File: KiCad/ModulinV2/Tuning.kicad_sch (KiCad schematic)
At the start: 26 parts

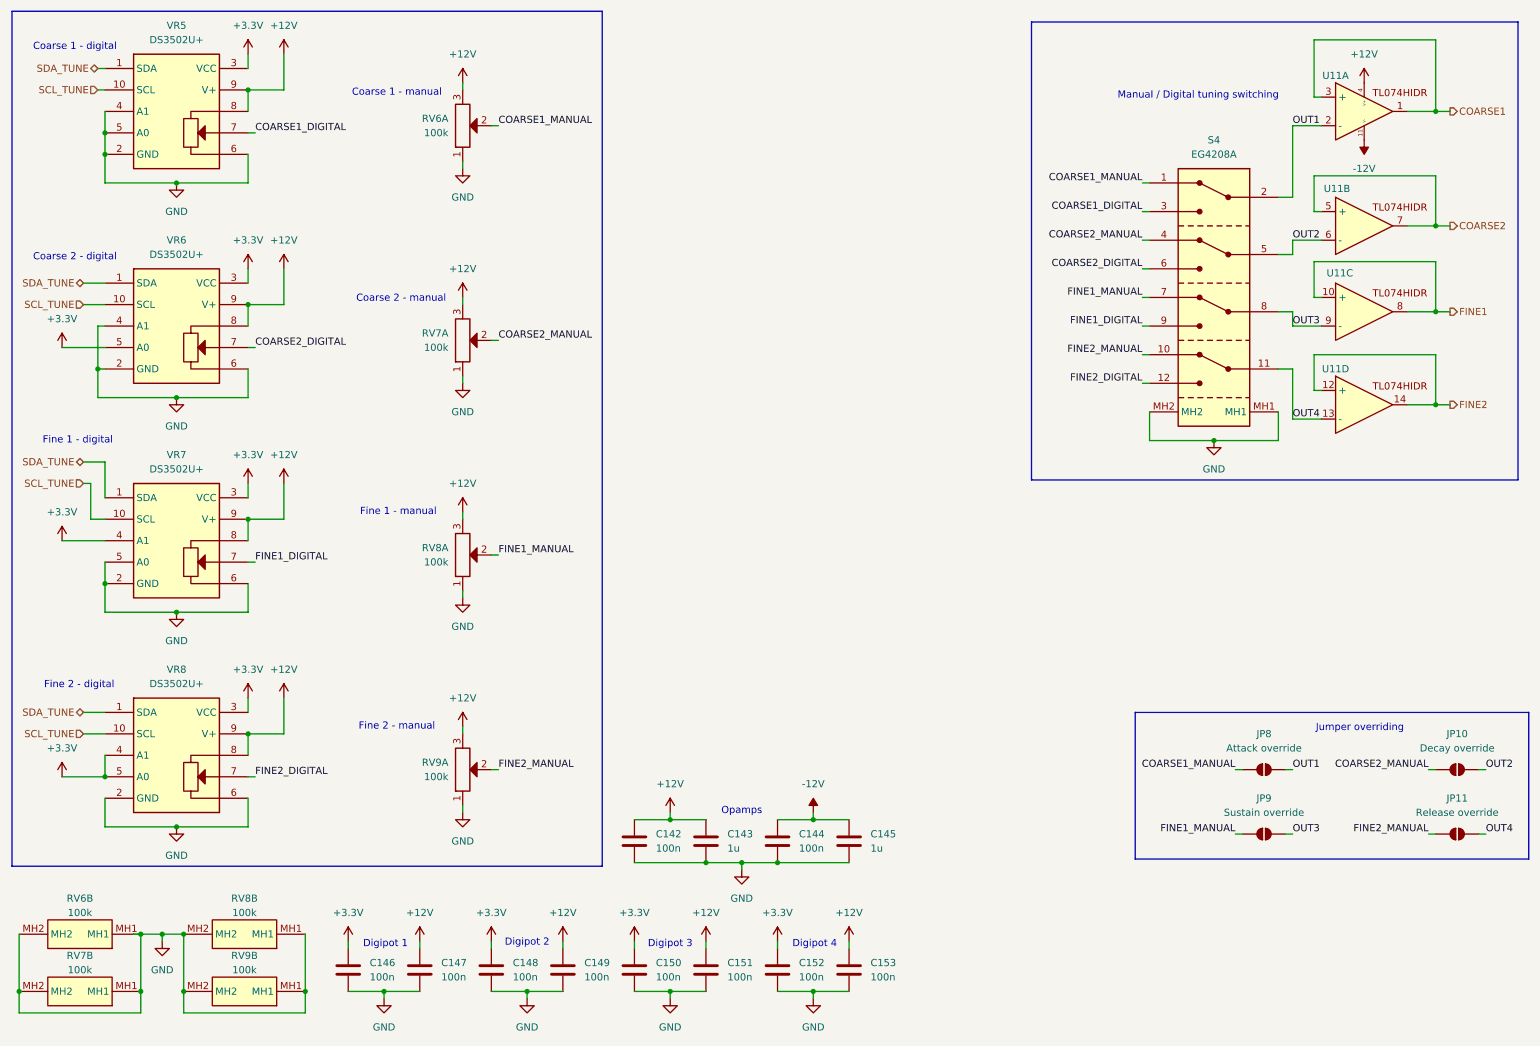
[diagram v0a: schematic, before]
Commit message: Added 4k7 pullups to I2C lines
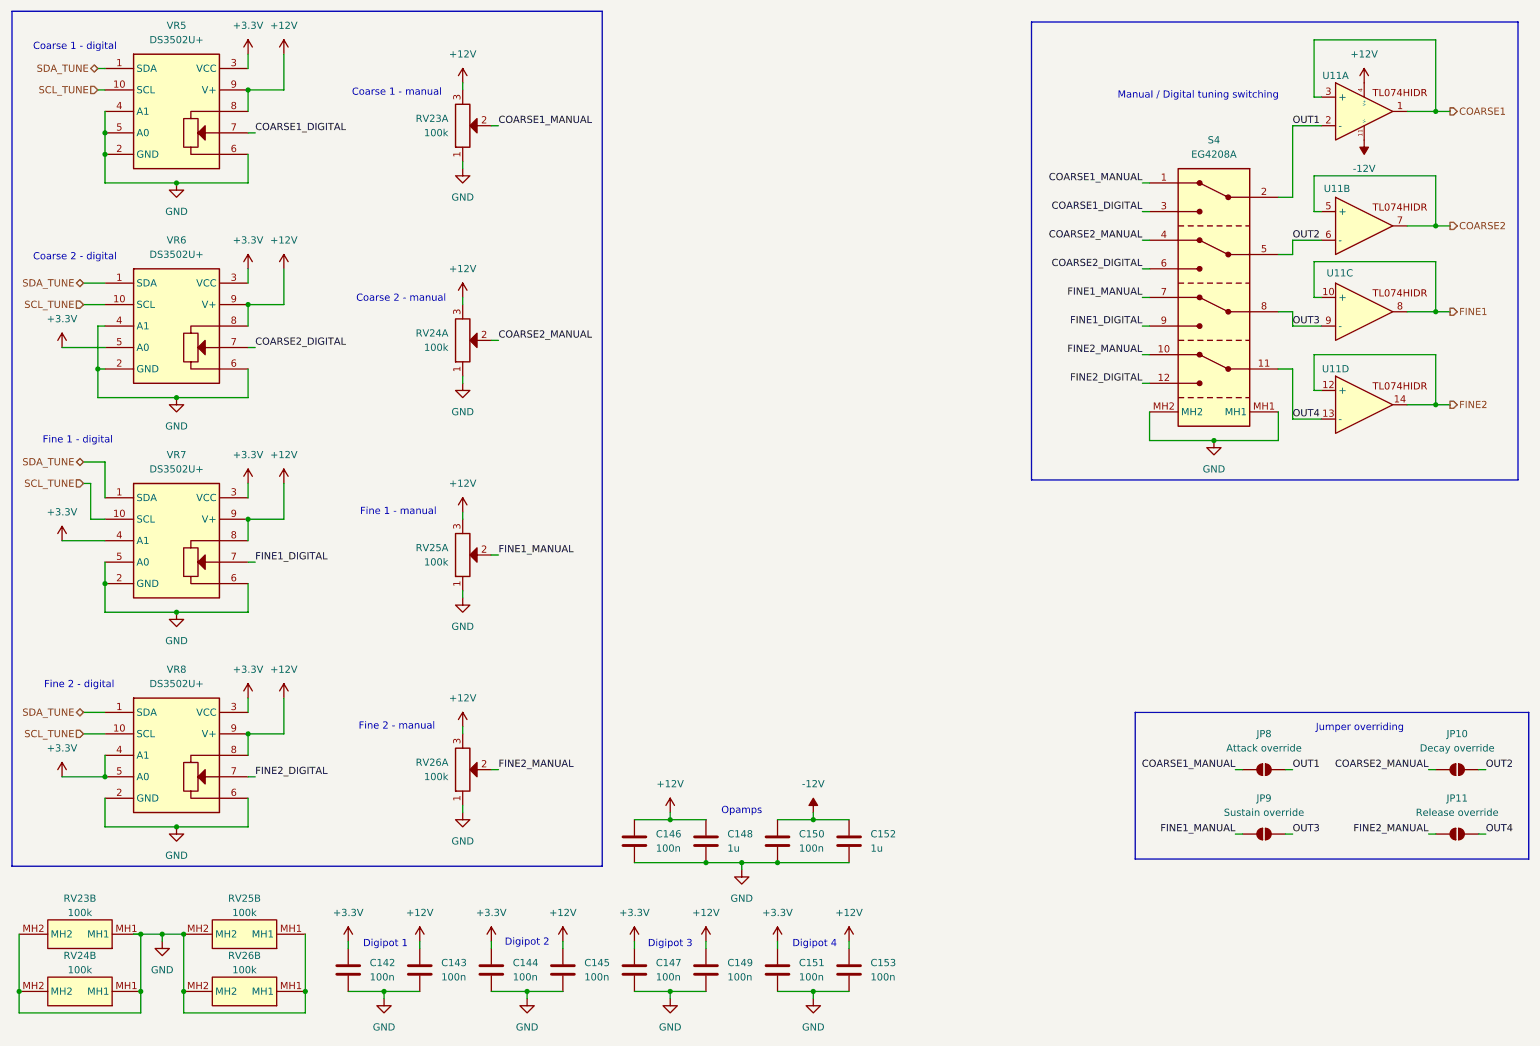
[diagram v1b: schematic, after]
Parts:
- renumbered C146 to C142, C147 to C143, C148 to C144, C149 to C145, C142 to C146, C150 to C147, C143 to C148, C151 to C149, C144 to C150, C152 to C151, C145 to C152, RV6 to RV23, RV7 to RV24, RV8 to RV25, RV9 to RV26

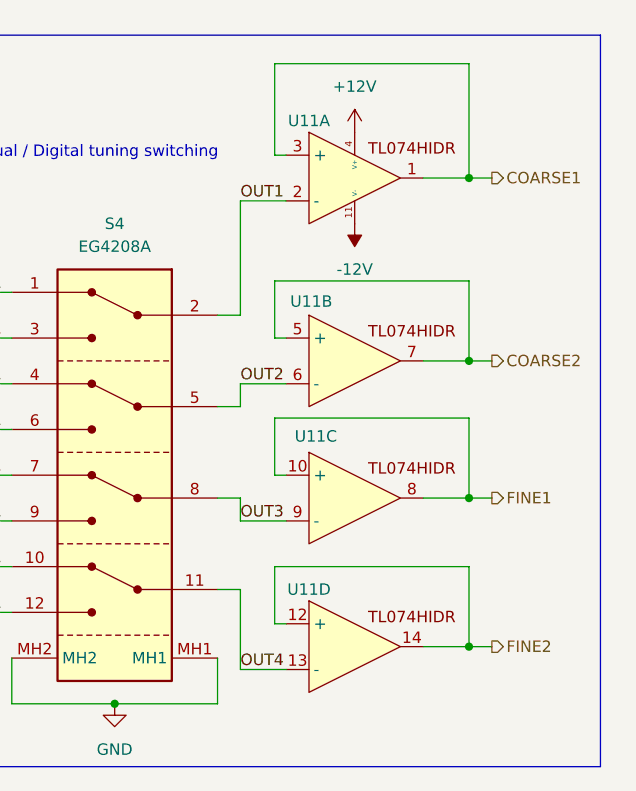
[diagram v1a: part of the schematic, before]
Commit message: Updated TL074 and 72 symbols
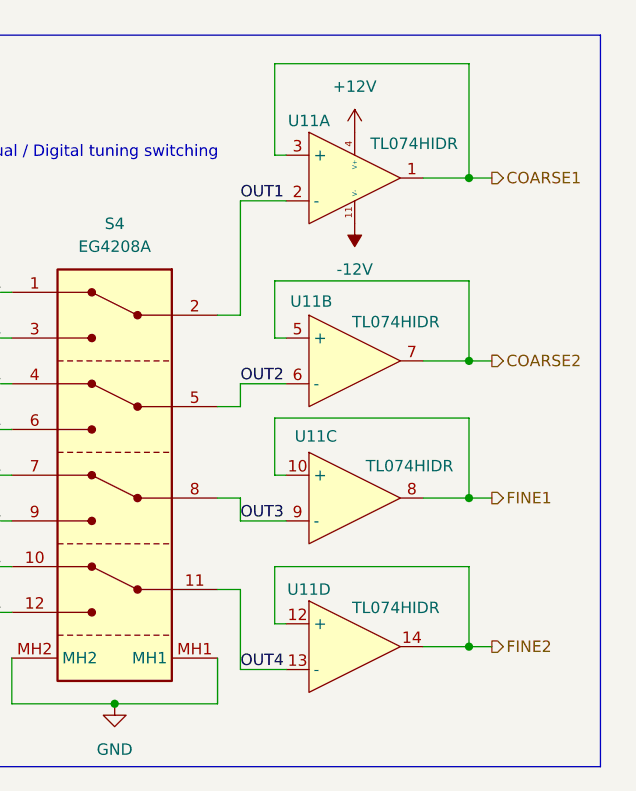
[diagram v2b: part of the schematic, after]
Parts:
- U11: value ~ -> TL074HIDR
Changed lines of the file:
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@@
 			)
 		)
-		(property "Value" "~"
-			(at 257.2155 45.72 0)
+		(property "Value" "TL074HIDR"
+			(at 258.572 47.752 0)
 			(effects
 				(font
@@
 			)
 		)
-		(property "Value" "~"
-			(at 257.2155 60.96 0)
+		(property "Value" "TL074HIDR"
+			(at 260.096 63.754 0)
 			(effects
 				(font
@@
 		(on_board yes)
 		(dnp no)
-		(fields_autoplaced yes)
 		(property "Reference" "U11"
 			(at 248.92 25.4 0)
@@
 			)
 		)
-		(property "Value" "~"
-			(at 266.7 28.5049 0)
+		(property "Value" "TL074HIDR"
+			(at 260.604 27.94 0)
 			(effects
 				(font
@@
 		(on_board yes)
 		(dnp no)
-		(fields_autoplaced yes)
 		(property "Reference" "U11"
 			(at 248.92 77.47 0)
@@
 			)
 		)
-		(property "Value" "~"
-			(at 257.2155 77.47 0)
+		(property "Value" "TL074HIDR"
+			(at 258.572 79.502 0)
 			(effects
 				(font

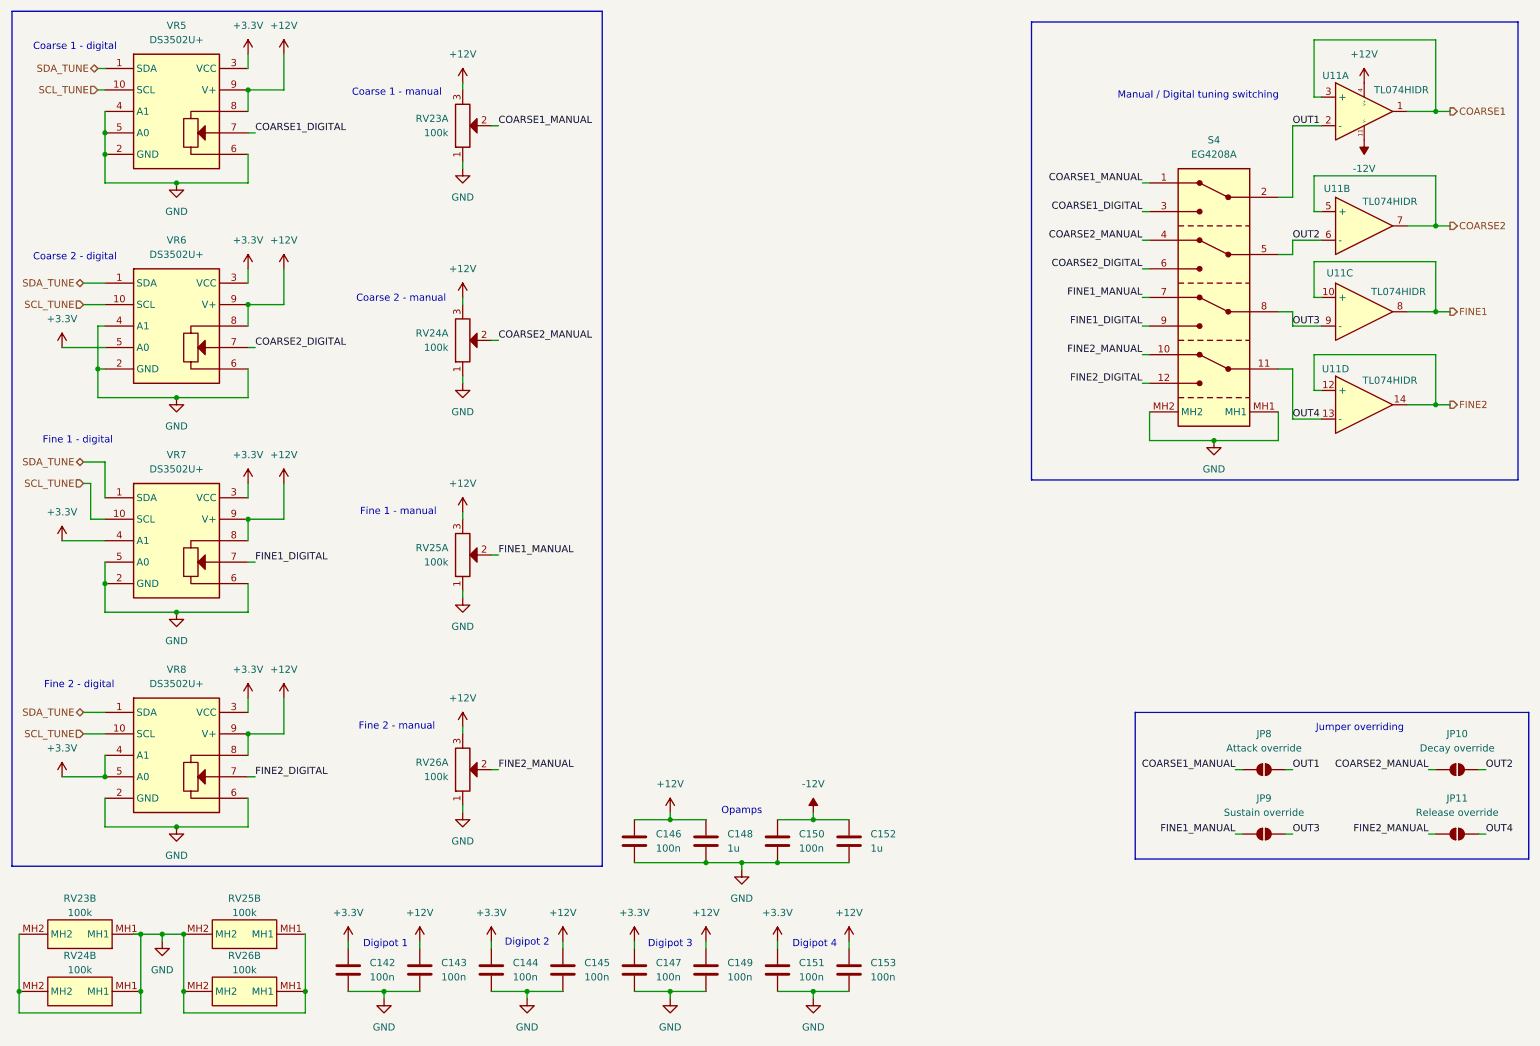
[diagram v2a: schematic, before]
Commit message: Fixed library issues and assigned most footprints
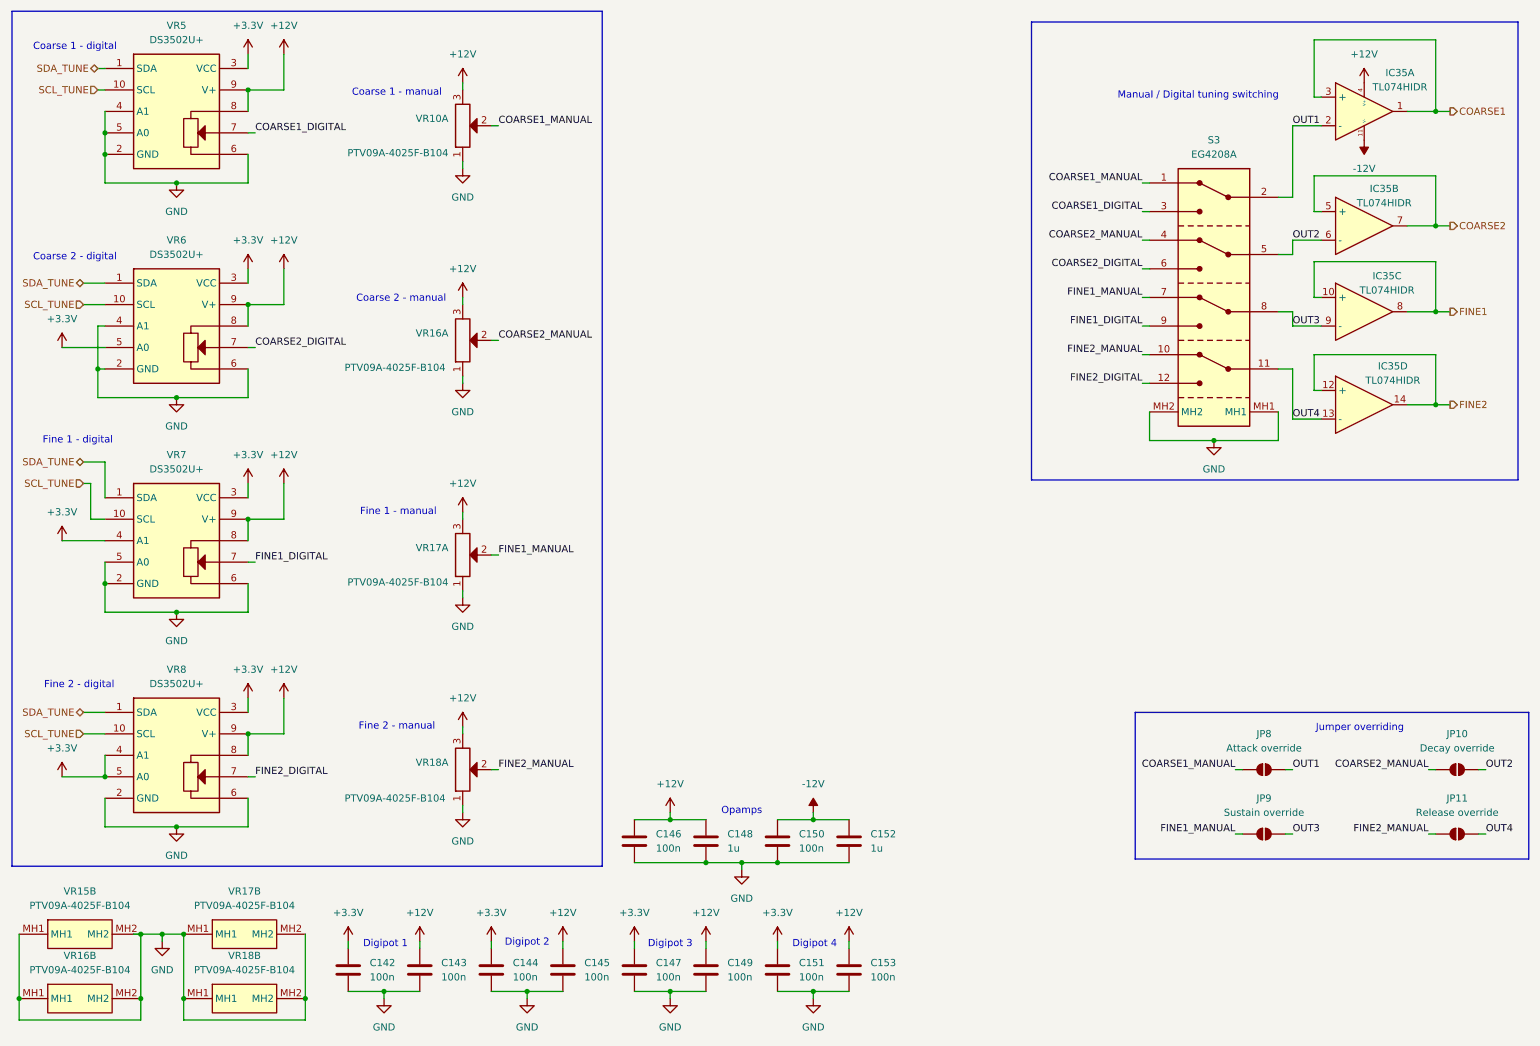
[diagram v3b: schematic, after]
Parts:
- removed RV23, RV24, RV25, RV26: 100k, symbol PTV09A-4025F-B104:PTV09A-4025F-B104_Alt
- removed S4: EG4208A, EG4208A, symbol EG4208A:EG4208A
- removed U11: TL074HIDR, symbol TL074HIDR:TL074HIDRx4
- removed VR5, VR6, VR7, VR8: DS3502U+, SOP50P490X110-10N, symbol DS3502U+:DS3502U+
- added IC35: TL074HIDR, SamacSys_Parts:SOIC127P600X175-14N, symbol SamacSys_Parts:TL074HIDR
- added S3: EG4208A, SamacSys_Parts:EG4208A, symbol SamacSys_Parts:EG4208A
- added VR10, VR15, VR16, VR17, VR18: PTV09A-4025F-B104, SamacSys_Parts:PTV09A4025FB104, symbol SamacSys_Parts:PTV09A-4025F-B104
- added VR5, VR6, VR7, VR8: DS3502U+, SamacSys_Parts:SOP50P490X110-10N, symbol SamacSys_Parts:DS3502U+
- JP10, JP11, JP8, JP9: footprint (none) -> Jumper:SolderJumper-2_P1.3mm_Open_TrianglePad1.0x1.5mm
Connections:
- net +12V: now also IC35.4 (V+), VR10.3, VR16.3, VR17.3, VR18.3, VR5.8, VR5.9 (V+), VR6.8, VR6.9 (V+), VR7.8, VR7.9 (V+), VR8.8, VR8.9 (V+)
- net +3.3V: now also VR5.3 (VCC), VR6.3 (VCC), VR6.5 (A0), VR7.3 (VCC), VR7.4 (A1), VR8.3 (VCC), VR8.4 (A1), VR8.5 (A0)
- net -12V: now also IC35.11 (V-)
- net COARSE1: now also IC35.1, IC35.3 (+)
- net COARSE1_DIGITAL: now also S3.3, VR5.7
- net COARSE1_MANUAL: now also S3.1, VR10.2
- net COARSE2: now also IC35.5 (+), IC35.7
- net COARSE2_DIGITAL: now also S3.6, VR6.7
- net COARSE2_MANUAL: now also S3.4, VR16.2
- net FINE1: now also IC35.10 (+), IC35.8
- net FINE1_DIGITAL: now also S3.9, VR7.7
- net FINE1_MANUAL: now also S3.7, VR17.2
- net FINE2: now also IC35.12 (+), IC35.14
- net FINE2_DIGITAL: now also S3.12, VR8.7
- net FINE2_MANUAL: now also S3.10, VR18.2
- net GND: now also S3.MH1, S3.MH2, VR10.1, VR15.MH1, VR15.MH2, VR16.1, VR16.MH1, VR16.MH2, VR17.1, VR17.MH1, VR17.MH2, VR18.1, VR18.MH1, VR18.MH2, VR5.2 (GND), VR5.4 (A1), VR5.5 (A0), VR5.6, VR6.2 (GND), VR6.4 (A1), VR6.6, VR7.2 (GND), VR7.5 (A0), VR7.6, VR8.2 (GND), VR8.6
- net OUT1: now also IC35.2 (-), S3.2
- net OUT2: now also IC35.6 (-), S3.5
- net OUT3: now also IC35.9 (-), S3.8
- net OUT4: now also IC35.13 (-), S3.11
- net SCL_TUNE: now also VR5.10 (SCL), VR6.10 (SCL), VR7.10 (SCL), VR8.10 (SCL)
- net SDA_TUNE: now also VR5.1 (SDA), VR6.1 (SDA), VR7.1 (SDA), VR8.1 (SDA)

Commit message: Changed switch for the boot and nrst. Fixed the GATE interface trigger
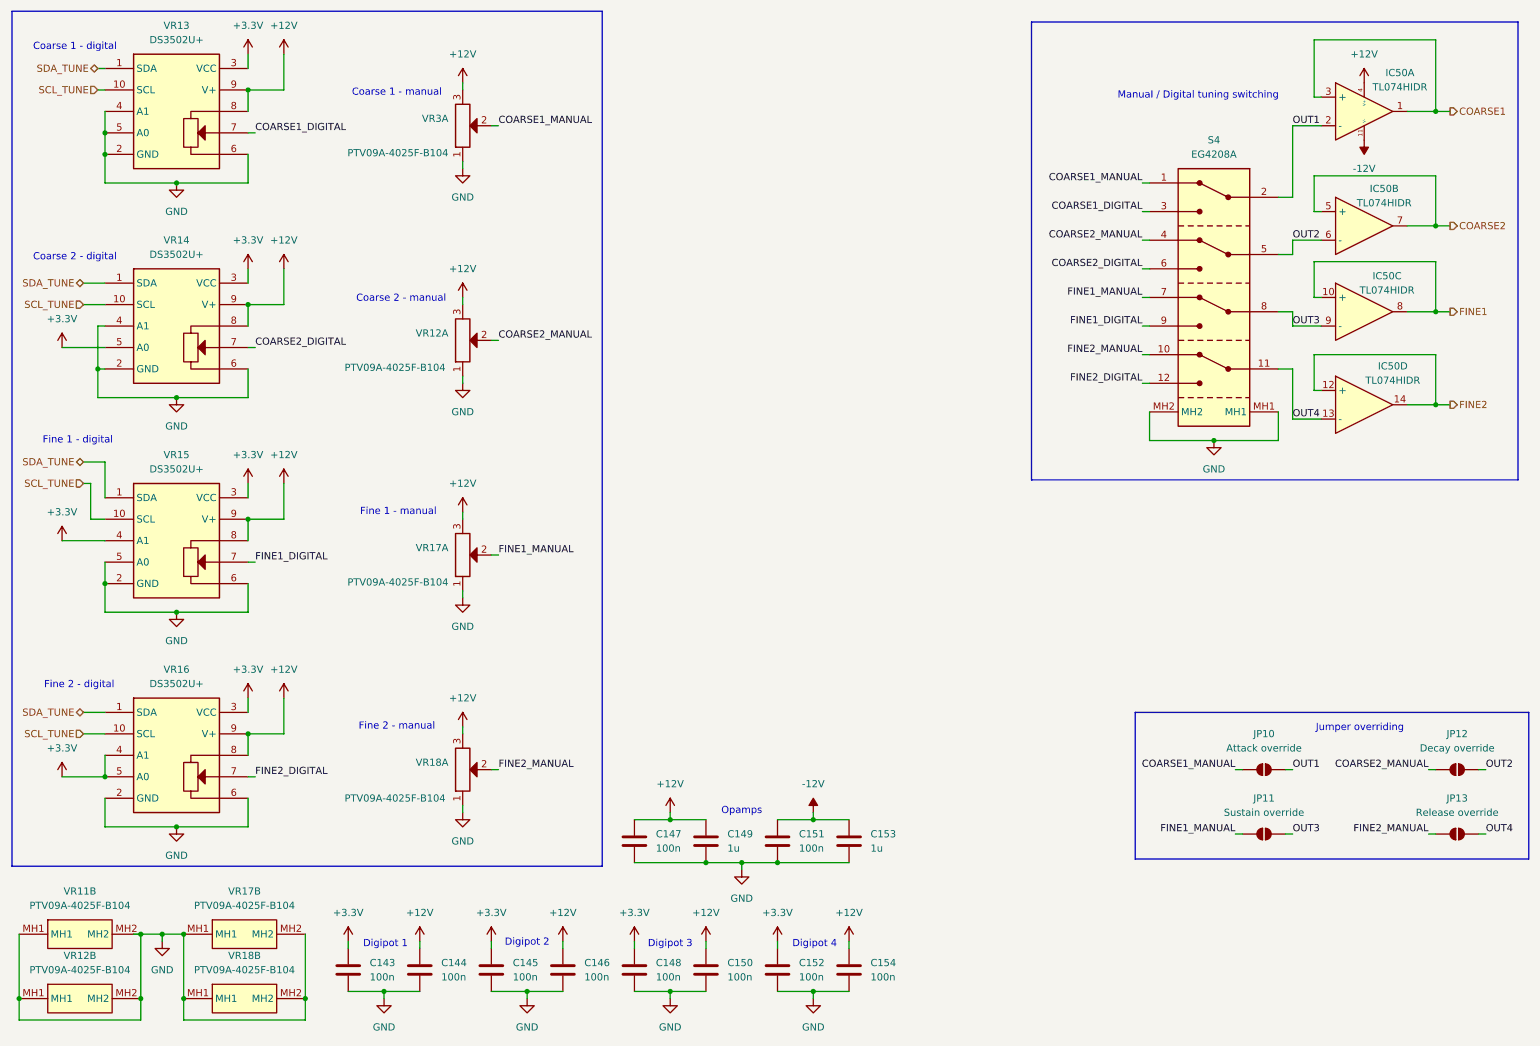
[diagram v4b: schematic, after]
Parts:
- renumbered C142 to C143, C143 to C144, C144 to C145, C145 to C146, C146 to C147, C147 to C148, C148 to C149, C149 to C150, C150 to C151, C151 to C152, C152 to C153, C153 to C154, IC35 to IC50, JP8 to JP10, JP9 to JP11, JP10 to JP12, JP11 to JP13, S3 to S4, VR15 to VR11, VR16 to VR12, VR5 to VR13, VR6 to VR14, VR7 to VR15, VR8 to VR16, VR10 to VR3
